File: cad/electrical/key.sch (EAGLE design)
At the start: 10 parts, among them U1 LD1117V50, U2 LM2903P

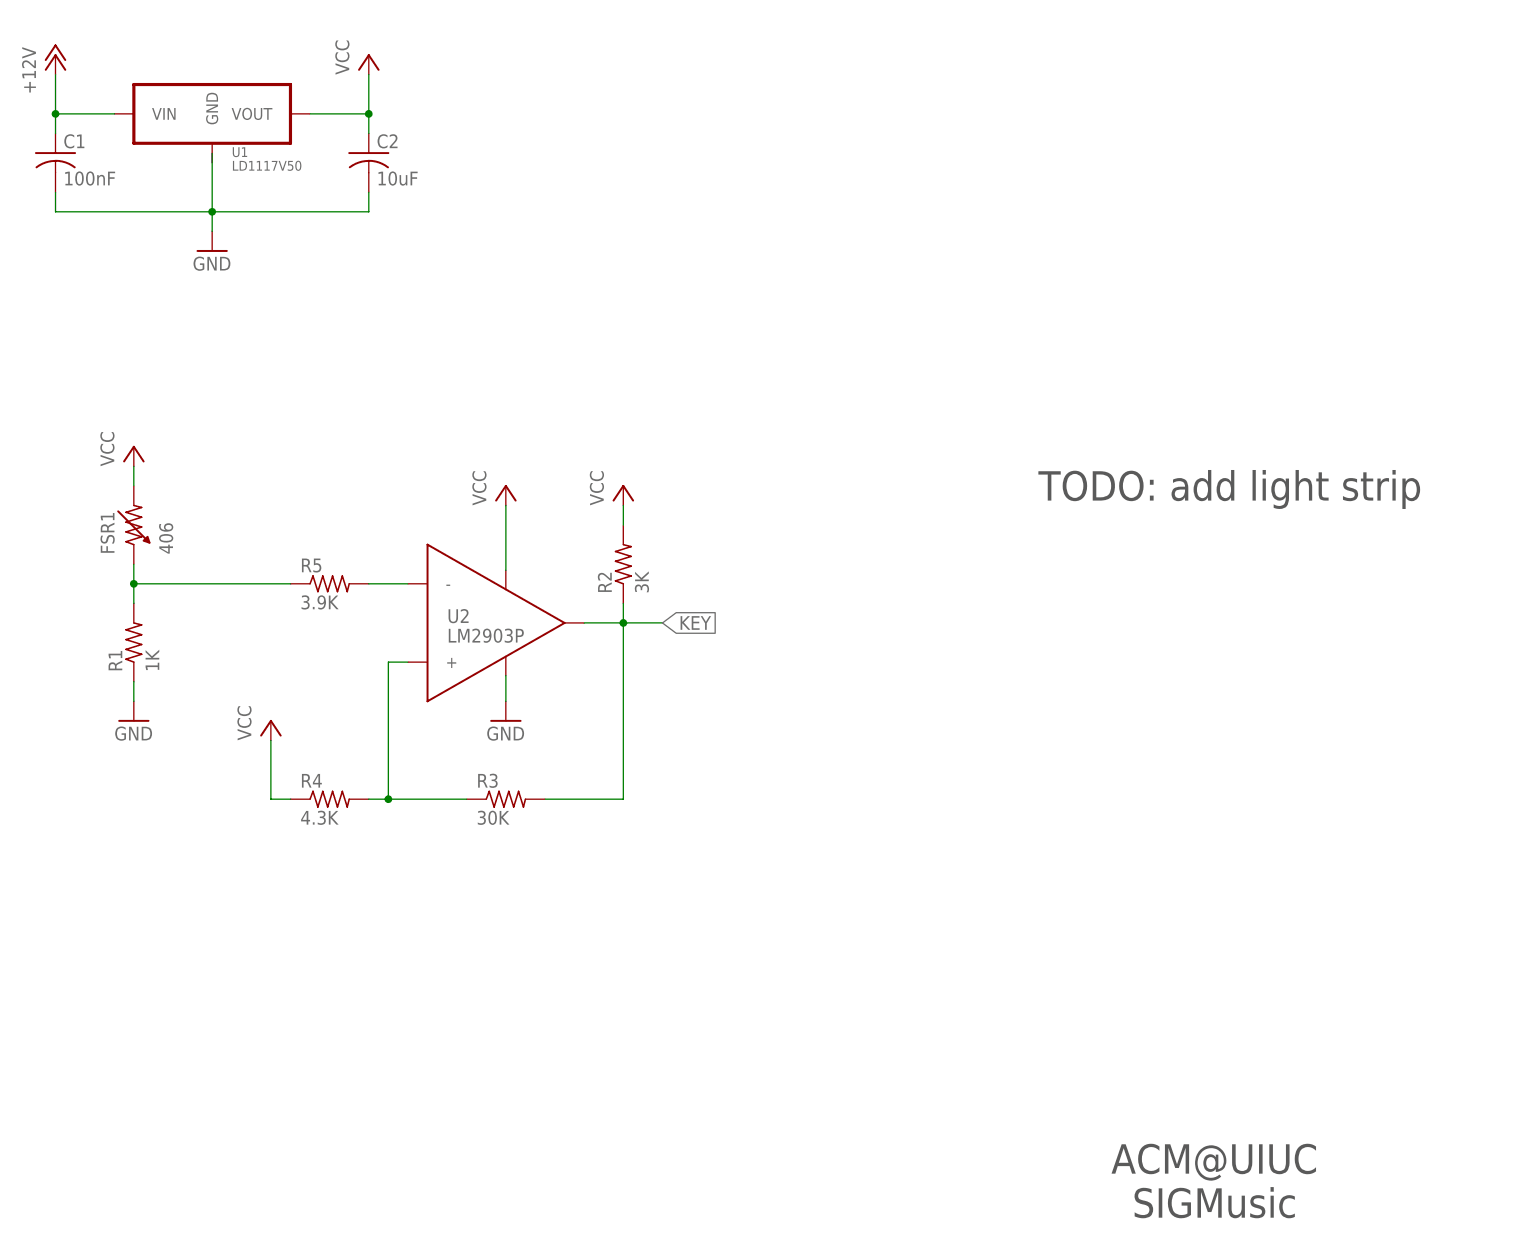
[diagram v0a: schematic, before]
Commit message: Updated schematic and BOMs
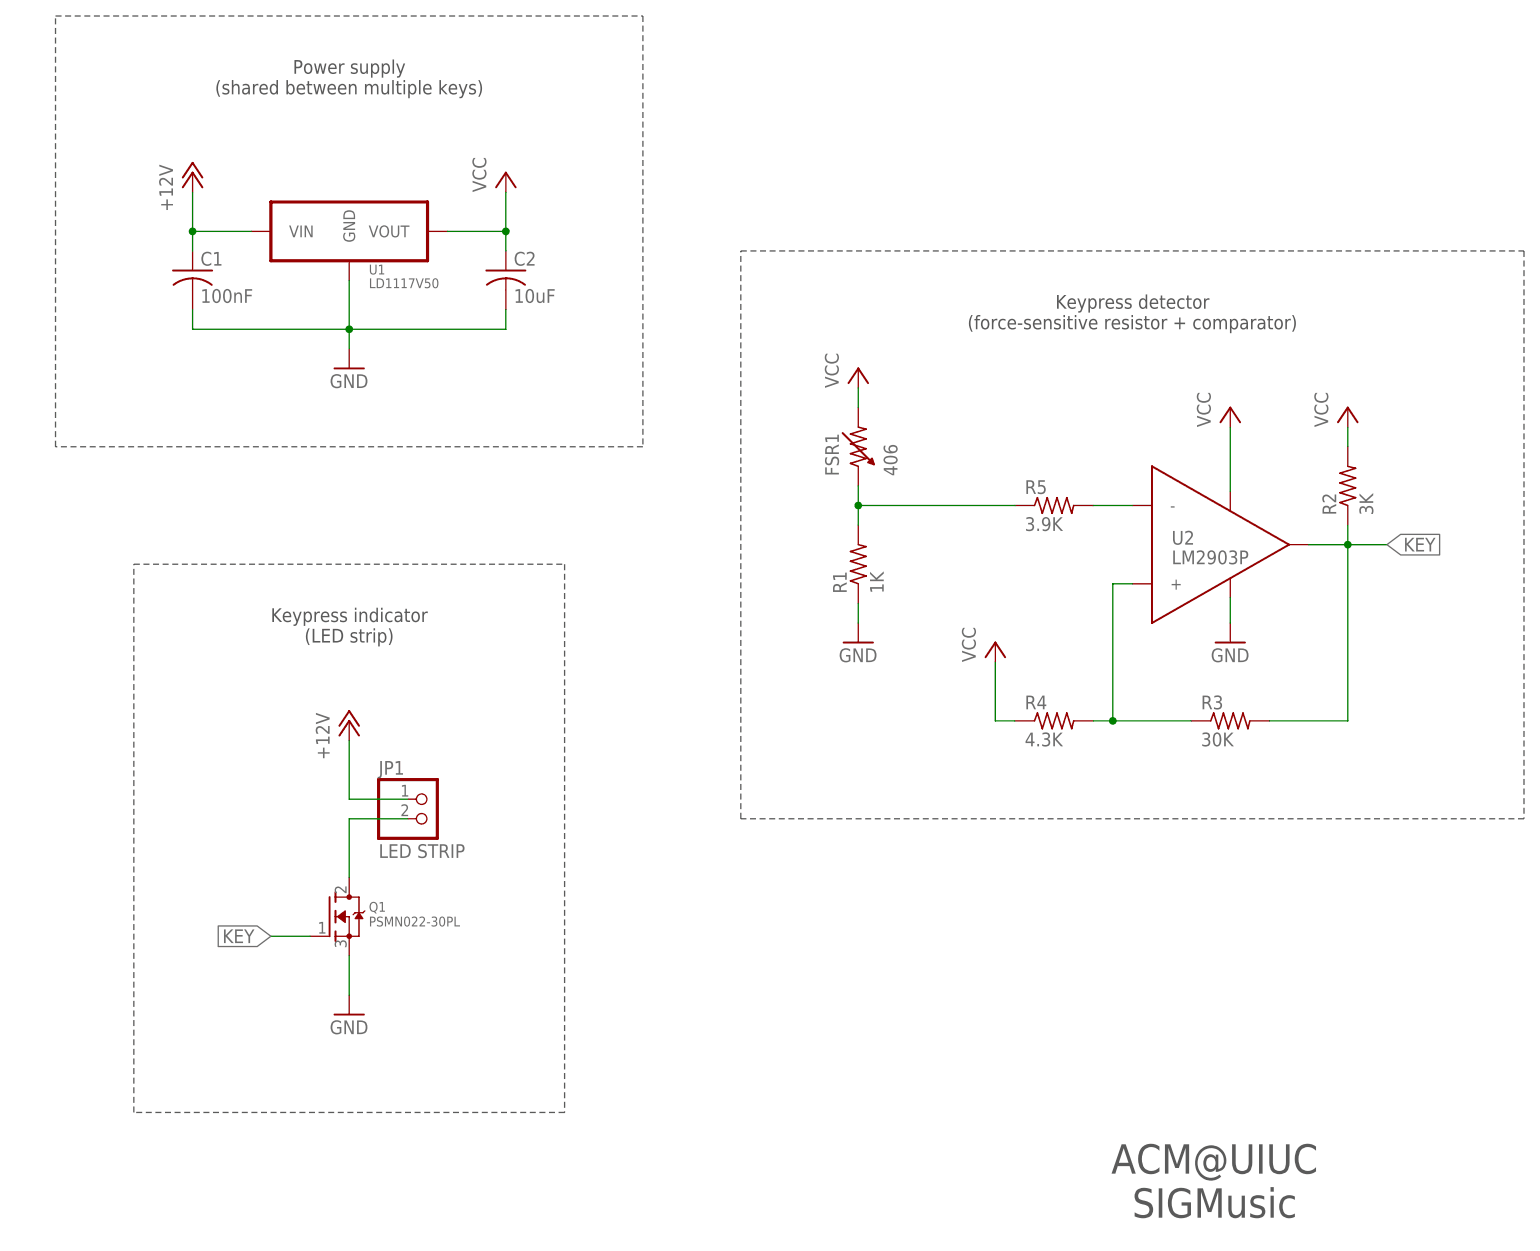
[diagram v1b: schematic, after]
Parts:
- added JP1: LED STRIP, pinhead:PINHD-1X2/90
- added Q1: PSMN022-30PL, adafruit:MOSFET-NGDS_TO220V
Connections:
- new net N$2: JP1.2, Q1.D
- net +12V: now also JP1.1
- net GND: now also Q1.S, U1.GND
- net KEY: now also Q1.G
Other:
- note added: "Keypress detector (force-sensitive resistor + comparator)"
- note added: "Keypress indicator (LED strip)"
- note added: "Power supply (shared between multiple keys)"
- note removed: "TODO: add light strip"
- moved on the sheet: C1, C2, FSR1, R1, R2, R3, R4, R5, U1, U2

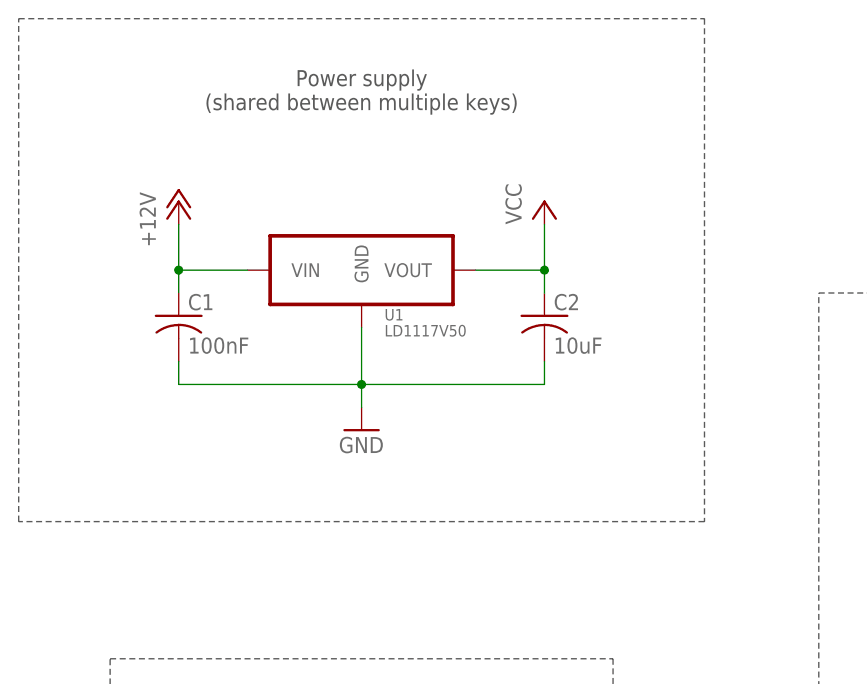
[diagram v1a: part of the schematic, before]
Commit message: Fixed incorrect text on schematic
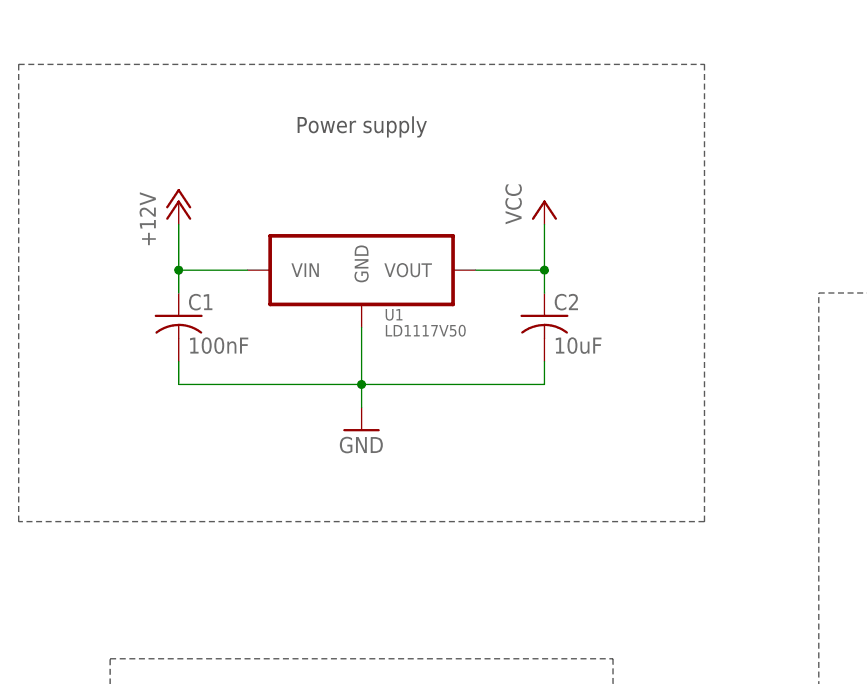
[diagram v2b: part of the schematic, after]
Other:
- note added: "Power supply"
- note removed: "Power supply (shared between multiple keys)"
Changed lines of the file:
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@@
 <text x="188.468" y="13.97" size="3.81" layer="97" align="center">ACM@UIUC
 SIGMusic</text>
-<wire x1="38.1" y1="165.1" x2="114.3" y2="165.1" width="0.1524" layer="97" style="longdash"/>
-<wire x1="114.3" y1="165.1" x2="114.3" y2="109.22" width="0.1524" layer="97" style="longdash"/>
+<wire x1="38.1" y1="160.02" x2="114.3" y2="160.02" width="0.1524" layer="97" style="longdash"/>
+<wire x1="114.3" y1="160.02" x2="114.3" y2="109.22" width="0.1524" layer="97" style="longdash"/>
 <wire x1="114.3" y1="109.22" x2="38.1" y2="109.22" width="0.1524" layer="97" style="longdash"/>
-<wire x1="38.1" y1="109.22" x2="38.1" y2="165.1" width="0.1524" layer="97" style="longdash"/>
-<text x="76.2" y="154.94" size="1.778" layer="97" align="bottom-center">Power supply
-(shared between multiple keys)</text>
+<wire x1="38.1" y1="109.22" x2="38.1" y2="160.02" width="0.1524" layer="97" style="longdash"/>
+<text x="76.2" y="152.4" size="1.778" layer="97" align="bottom-center">Power supply</text>
 <wire x1="127" y1="134.62" x2="228.6" y2="134.62" width="0.1524" layer="97" style="longdash"/>
 <wire x1="228.6" y1="134.62" x2="228.6" y2="60.96" width="0.1524" layer="97" style="longdash"/>

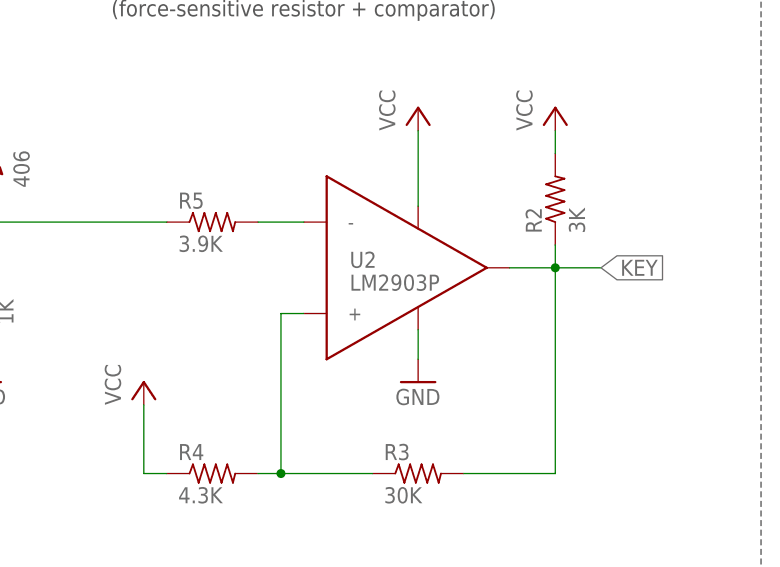
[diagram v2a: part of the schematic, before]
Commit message: Fixed comparator part
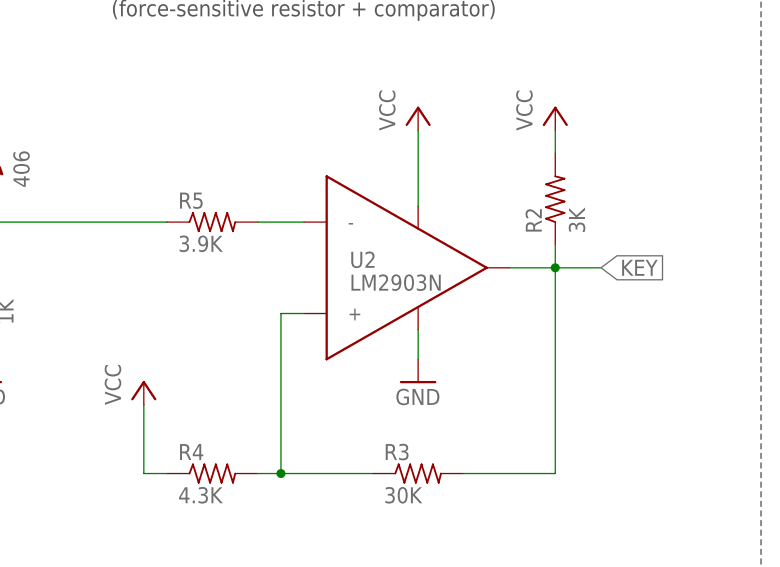
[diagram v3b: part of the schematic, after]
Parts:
- U2: value LM2903P -> LM2903N
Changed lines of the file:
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@@
 <part name="P+3" library="supply1" deviceset="VCC" device=""/>
 <part name="R1" library="rcl" deviceset="R-US_" device="0207/10" value="1K"/>
-<part name="U2" library="my-custom" deviceset="LM2903P" device="" value="LM2903P"/>
+<part name="U2" library="my-custom" deviceset="LM2903P" device="" value="LM2903N"/>
 <part name="P+4" library="supply1" deviceset="VCC" device=""/>
 <part name="GND3" library="supply1" deviceset="GND" device=""/>

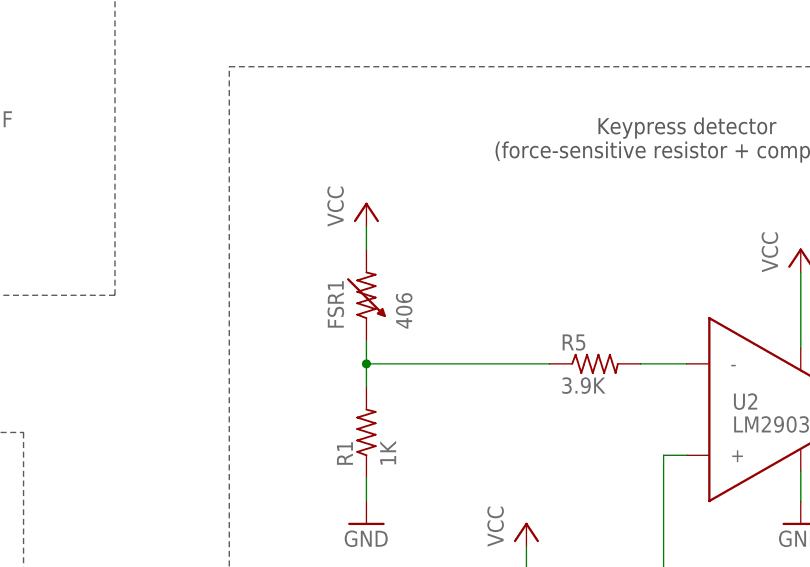
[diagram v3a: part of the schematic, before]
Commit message: Clarified FSR value
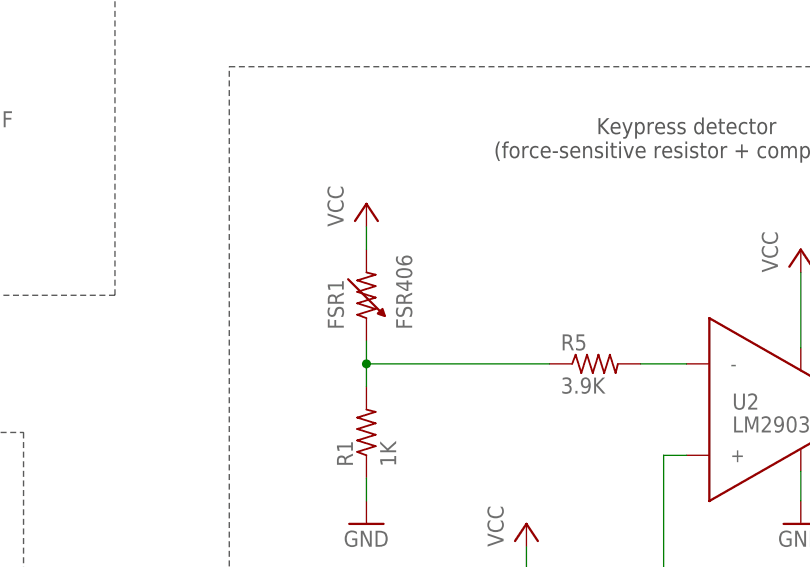
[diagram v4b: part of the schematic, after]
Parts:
- FSR1: value 406 -> FSR406
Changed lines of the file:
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@@
 <parts>
 <part name="FRAME1" library="frames" deviceset="A4L-LOC" device=""/>
-<part name="FSR1" library="my-custom" deviceset="FSR-SQUARE" device="" value="406"/>
+<part name="FSR1" library="my-custom" deviceset="FSR-SQUARE" device="" value="FSR406"/>
 <part name="U1" library="my-custom" deviceset="LD1117" device="" value="LD1117V50"/>
 <part name="P+1" library="supply1" deviceset="VCC" device=""/>
